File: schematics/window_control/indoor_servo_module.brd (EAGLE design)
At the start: 48.2 x 59.4 mm, 32 parts, among them J1 MTR-SERVO-FS5103B, J2 GND, J3 +5V, J4 OUTDOOR_SIGNAL, J5 J2, J6 J2, J7 J2, Q2 2N3904, Q3 2N3906BU, Q4 2N3904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

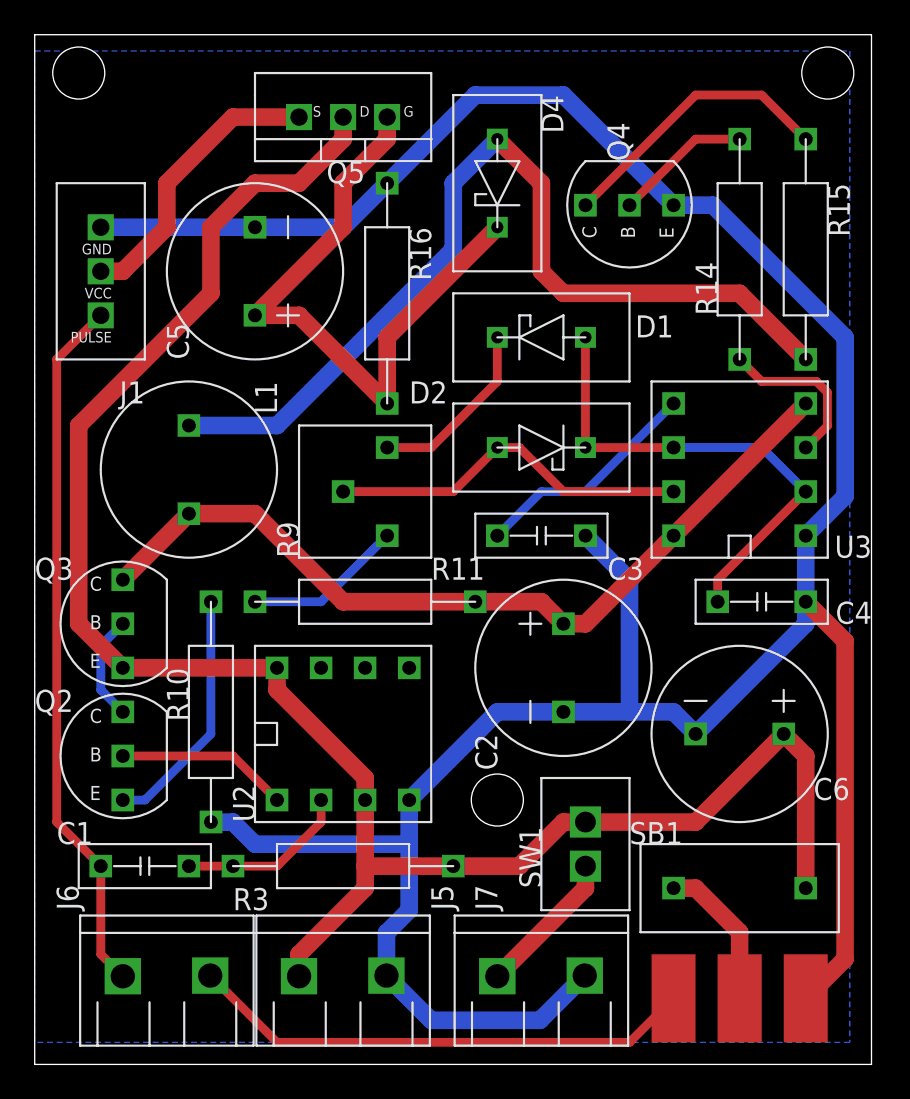
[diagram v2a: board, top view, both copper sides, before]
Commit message: Connectors changed
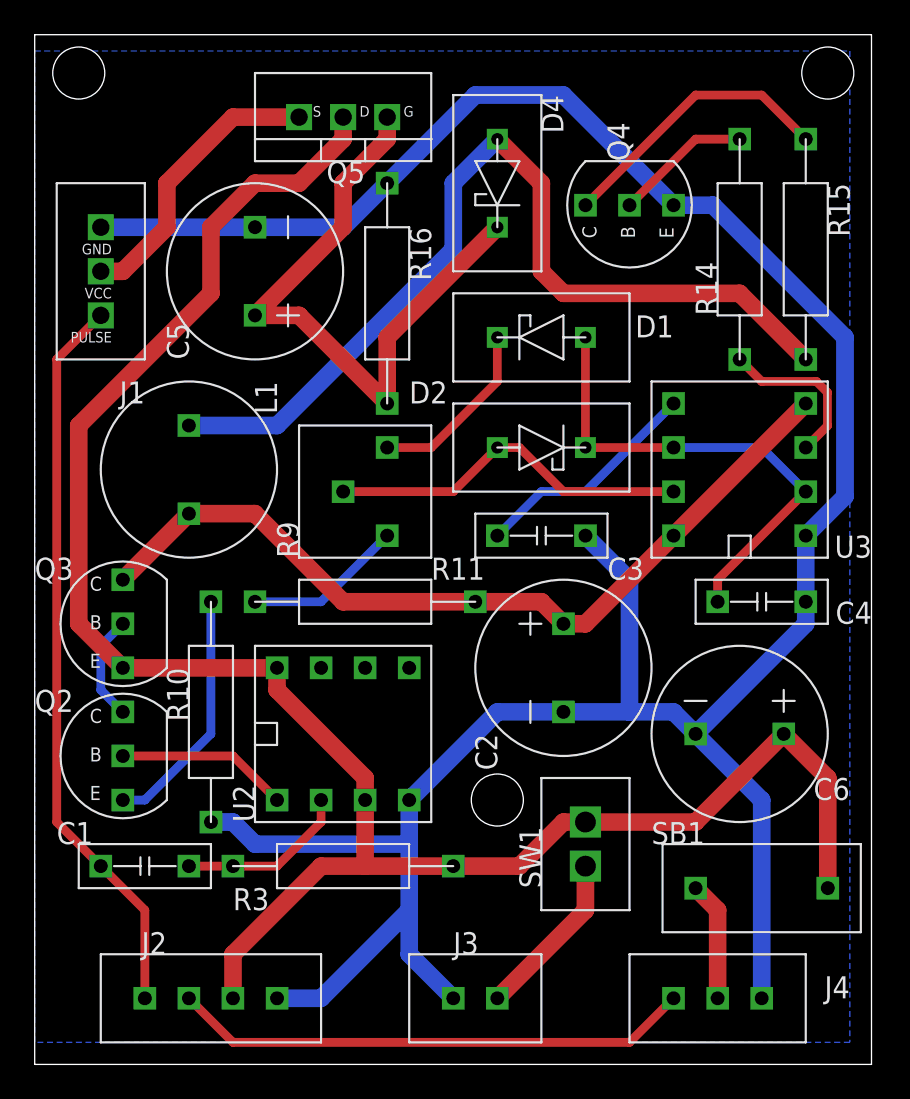
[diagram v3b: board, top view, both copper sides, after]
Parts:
- removed J5, J6, J7: J2, my_devices:J2
- J2: value GND -> JST-XH2.54-4P; device my_devices:J_SMD -> my_devices:JST-XH254-4P
- J3: value +5V -> JST-XH2.54-2P; device my_devices:J_SMD -> my_devices:JST-XH254-2P
- J4: value OUTDOOR_SIGNAL -> JST-XH2.54-3P; device my_devices:J_SMD -> my_devices:JST-XH254-3P
- moved J2 34.3 mm to (47.0, -5.08), turned to 180 degrees
- moved J3 15.2 mm to (62.2, -5.08), turned to 0 degrees
- moved J4 2.54 mm to (76.2, -5.08), turned to 180 degrees
- moved SB1 1.27 mm to (78.7, 1.27)
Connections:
- removed net N$5: J3.PIN, SB1.P$1
- new net N$4: J4.PIN2, SB1.P$1
- net +5V: now also J2.PIN2; no longer J5.PIN_1
- net GND: now also J2.PIN1, J3.PIN1, J4.PIN1; no longer J2.PIN, J5.PIN_2, J7.PIN_2
- net N$3: now also J3.PIN2; no longer J7.PIN_1
- net OUTDOOR_SIGNAL: now also J2.PIN3, J4.PIN3; no longer J4.PIN, J6.PIN_2
- net SERVO_PWM_CONTROL: now also J2.PIN4; no longer J6.PIN_1
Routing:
- net GND: track 169.6 -> 159.6 mm
- net N$5: track 8.74 -> 0.00 mm
- net N$4: track 0.00 -> 6.88 mm
- net +5V: track 107.7 -> 112.5 mm
- net SERVO_PWM_CONTROL: track 40.7 -> 42.5 mm
- net N$3: track 8.45 -> 9.72 mm
- net OUTDOOR_SIGNAL: track 29.4 -> 30.0 mm
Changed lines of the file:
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@@
 <attribute name="NAME" x="43.18" y="30.48" size="1.27" layer="21" rot="R180"/>
-</element>
-<element name="J2" library="my_devices" package="J_SMD" value="GND" x="81.28" y="-5.08" smashed="yes" rot="R90"/>
-<element name="J3" library="my_devices" package="J_SMD" value="+5V" x="77.47" y="-5.08" smashed="yes" rot="R90"/>
-<element name="J4" library="my_devices" package="J_SMD" value="OUTDOOR_SIGNAL" x="73.66" y="-5.08" smashed="yes" rot="R90"/>
-<element name="J5" library="my_devices" package="J2" value="J2" x="54.61" y="-3.81" smashed="yes" rot="R90">
-<attribute name="NAME" x="60.96" y="0" size="1.27" layer="21" rot="R90"/>
-</element>
-<element name="J6" library="my_devices" package="J2" value="J2" x="44.45" y="-3.81" smashed="yes" rot="R90">
-<attribute name="NAME" x="39.37" y="0" size="1.27" layer="21" rot="R90"/>
-</element>
-<element name="J7" library="my_devices" package="J2" value="J2" x="66.04" y="-3.81" smashed="yes" rot="R90">
-<attribute name="NAME" x="63.5" y="0" size="1.27" layer="21" rot="R90"/>
 </element>
 <element name="L1" library="my_devices" package="L-RLB0914" value="RLB0914-102KL, 1000 uH" x="45.72" y="25.4" smashed="yes" rot="R270">
@@
 <attribute name="NAME" x="52.07" y="20.32" size="1.27" layer="21" rot="R90"/>
 </element>
-<element name="SB1" library="my_devices" package="SB-NC" value="KLS7-DS-01-B-00" x="77.47" y="1.27" smashed="yes">
-<attribute name="NAME" x="71.12" y="3.81" size="1.27" layer="21"/>
+<element name="SB1" library="my_devices" package="SB-NC" value="KLS7-DS-01-B-00" x="78.74" y="1.27" smashed="yes">
+<attribute name="NAME" x="72.39" y="3.81" size="1.27" layer="21"/>
 </element>
 <element name="SW1" library="my_devices" package="SWITCH" value="SWITCH" x="68.58" y="3.81" smashed="yes" rot="R90">
@@
 <element name="D2" library="my_devices" package="D_SCHOTTKY" value="BAT41" x="66.04" y="26.67" smashed="yes">
 <attribute name="NAME" x="58.42" y="29.21" size="1.27" layer="21"/>
+</element>
+<element name="J4" library="my_devices" package="JST-XH254-3P" value="JST-XH2.54-3P" x="76.2" y="-5.08" smashed="yes" rot="R180">
+<attribute name="NAME" x="83.82" y="-3.81" size="1.27" layer="21" rot="R180"/>
+</element>
+<element name="J2" library="my_devices" package="JST-XH254-4P" value="JST-XH2.54-4P" x="46.99" y="-5.08" smashed="yes" rot="R180">
+<attribute name="NAME" x="44.45" y="-1.27" size="1.27" layer="21" rot="R180"/>
+</element>
+<element name="J3" library="my_devices" package="JST-XH254-2P" value="JST-XH2.54-2P" x="62.23" y="-5.08" smashed="yes">
+<attribute name="NAME" x="60.96" y="-2.54" size="1.27" layer="21"/>
 </element>
 </elements>
@@
 <contactref element="R3" pad="P$2"/>
 <contactref element="U2" pad="PIN_3"/>
-<contactref element="J5" pad="PIN_1"/>
 <contactref element="SW1" pad="P$2"/>
 <contactref element="SB1" pad="P$2"/>
 <contactref element="C6" pad="PIN_PLUS"/>
-<wire x1="81.28" y1="1.27" x2="81.28" y2="8.89" width="1.016" layer="1"/>
-<wire x1="81.28" y1="8.89" x2="80.01" y2="10.16" width="1.016" layer="1"/>
+<wire x1="82.55" y1="1.27" x2="82.55" y2="7.62" width="1.016" layer="1"/>
+<wire x1="82.55" y1="7.62" x2="80.01" y2="10.16" width="1.016" layer="1"/>
 <wire x1="68.58" y1="5.08" x2="74.93" y2="5.08" width="1.016" layer="1"/>
 <wire x1="74.93" y1="5.08" x2="80.01" y2="10.16" width="1.016" layer="1"/>
-<wire x1="52.07" y1="-3.81" x2="52.07" y2="-2.54" width="1.016" layer="1"/>
-<wire x1="52.07" y1="-2.54" x2="55.88" y2="1.27" width="1.016" layer="1"/>
-<wire x1="55.88" y1="1.27" x2="55.88" y2="2.54" width="1.016" layer="1"/>
 <wire x1="55.88" y1="2.54" x2="55.88" y2="6.35" width="1.016" layer="1"/>
 <wire x1="60.96" y1="2.54" x2="55.88" y2="2.54" width="1.016" layer="1"/>
@@
 <wire x1="64.77" y1="2.54" x2="67.31" y2="5.08" width="1.016" layer="1"/>
 <wire x1="67.31" y1="5.08" x2="68.58" y2="5.08" width="1.016" layer="1"/>
+<contactref element="J2" pad="PIN2"/>
+<wire x1="55.88" y1="2.54" x2="53.34" y2="2.54" width="1.016" layer="1"/>
+<wire x1="53.34" y1="2.54" x2="48.26" y2="-2.54" width="1.016" layer="1"/>
+<wire x1="48.26" y1="-2.54" x2="48.26" y2="-5.08" width="1.016" layer="1"/>
 </signal>
 <signal name="GND">
@@
 <contactref element="C2" pad="PIN_GND"/>
 <contactref element="U3" pad="PIN_1"/>
-<contactref element="J2" pad="PIN"/>
-<contactref element="J5" pad="PIN_2"/>
-<contactref element="J7" pad="PIN_2"/>
 <contactref element="C6" pad="PIN_GND"/>
-<wire x1="57.11" y1="-3.77" x2="59.69" y2="-6.35" width="1.016" layer="16"/>
-<wire x1="65.96" y1="-6.35" x2="68.54" y2="-3.77" width="1.016" layer="16"/>
-<wire x1="59.69" y1="-6.35" x2="65.96" y2="-6.35" width="1.016" layer="16"/>
-<wire x1="57.11" y1="-3.77" x2="57.11" y2="-1.31" width="1.016" layer="16"/>
-<wire x1="57.11" y1="-1.31" x2="58.42" y2="0" width="1.016" layer="16"/>
-<wire x1="58.42" y1="0" x2="58.42" y2="3.81" width="1.016" layer="16"/>
+<wire x1="58.42" y1="3.81" x2="58.42" y2="0" width="1.016" layer="16"/>
 <wire x1="58.42" y1="3.81" x2="58.42" y2="6.35" width="1.016" layer="16"/>
 <wire x1="46.99" y1="5.08" x2="48.26" y2="5.08" width="1.016" layer="16"/>
@@
 <wire x1="49.53" y1="3.81" x2="58.42" y2="3.81" width="1.016" layer="16"/>
 <wire x1="74.93" y1="10.16" x2="81.28" y2="16.51" width="1.016" layer="16"/>
-<wire x1="81.28" y1="16.51" x2="81.28" y2="17.78" width="1.016" layer="16"/>
+<wire x1="81.28" y1="17.78" x2="81.28" y2="16.51" width="1.016" layer="16"/>
 <wire x1="81.28" y1="17.78" x2="81.28" y2="21.59" width="1.016" layer="16"/>
 <wire x1="57.15" y1="41.91" x2="54.61" y2="39.37" width="1.016" layer="16"/>
@@
 <wire x1="83.546" y1="33.02" x2="75.926" y2="40.64" width="1.016" layer="16"/>
 <wire x1="75.926" y1="40.64" x2="73.66" y2="40.64" width="1.016" layer="16"/>
-<wire x1="81.28" y1="17.78" x2="83.546" y2="15.514" width="1.016" layer="1"/>
-<wire x1="83.546" y1="-2.814" x2="81.28" y2="-5.08" width="1.016" layer="1"/>
-<wire x1="83.546" y1="15.514" x2="83.546" y2="-2.814" width="1.016" layer="1"/>
 <wire x1="58.42" y1="6.35" x2="63.5" y2="11.43" width="1.016" layer="16"/>
 <wire x1="63.5" y1="11.43" x2="67.31" y2="11.43" width="1.016" layer="16"/>
@@
 <vertex x="36.83" y="-7.62"/>
 </polygon>
+<contactref element="J4" pad="PIN1"/>
+<contactref element="J2" pad="PIN1"/>
+<contactref element="J3" pad="PIN1"/>
+<wire x1="58.42" y1="0" x2="53.34" y2="-5.08" width="1.016" layer="16"/>
+<wire x1="53.34" y1="-5.08" x2="50.8" y2="-5.08" width="1.016" layer="16"/>
+<wire x1="58.42" y1="0" x2="58.42" y2="-2.54" width="1.016" layer="16"/>
+<wire x1="58.42" y1="-2.54" x2="60.96" y2="-5.08" width="1.016" layer="16"/>
+<wire x1="74.93" y1="10.16" x2="78.74" y2="6.35" width="1.016" layer="16"/>
+<wire x1="78.74" y1="6.35" x2="78.74" y2="-5.08" width="1.016" layer="16"/>
 </signal>
 <signal name="SERVO_PWM_CONTROL">
 <contactref element="J1" pad="PULSE"/>
 <contactref element="C1" pad="P$1"/>
-<contactref element="J6" pad="PIN_1"/>
-<wire x1="41.91" y1="-3.81" x2="40.64" y2="-2.54" width="0.508" layer="1"/>
-<wire x1="40.64" y1="-2.54" x2="40.64" y2="2.54" width="0.508" layer="1"/>
 <wire x1="40.64" y1="2.54" x2="38.1" y2="5.08" width="0.508" layer="1"/>
 <wire x1="38.1" y1="5.08" x2="38.1" y2="31.75" width="0.508" layer="1"/>
 <wire x1="38.1" y1="31.75" x2="40.64" y2="34.29" width="0.508" layer="1"/>
+<contactref element="J2" pad="PIN4"/>
+<wire x1="40.64" y1="2.54" x2="43.18" y2="0" width="0.508" layer="1"/>
+<wire x1="43.18" y1="0" x2="43.18" y2="-5.08" width="0.508" layer="1"/>
 </signal>
 <signal name="N$39">
@@
 </signal>
 <signal name="OUTDOOR_SIGNAL">
-<contactref element="J4" pad="PIN"/>
-<contactref element="J6" pad="PIN_2"/>
-<wire x1="46.95" y1="-3.77" x2="50.8" y2="-7.62" width="0.508" layer="1"/>
-<wire x1="50.8" y1="-7.62" x2="71.12" y2="-7.62" width="0.508" layer="1"/>
+<contactref element="J4" pad="PIN3"/>
+<contactref element="J2" pad="PIN3"/>
+<wire x1="45.72" y1="-5.08" x2="48.26" y2="-7.62" width="0.508" layer="1"/>
 <wire x1="71.12" y1="-7.62" x2="73.66" y2="-5.08" width="0.508" layer="1"/>
+<wire x1="48.26" y1="-7.62" x2="71.12" y2="-7.62" width="0.508" layer="1"/>
 </signal>
 <signal name="N$3">
-<contactref element="J7" pad="PIN_1"/>
 <contactref element="SW1" pad="P$1"/>
-<wire x1="68.58" y1="2.54" x2="68.58" y2="1.27" width="1.016" layer="1"/>
-<wire x1="68.58" y1="1.27" x2="63.5" y2="-3.81" width="1.016" layer="1"/>
-</signal>
-<signal name="N$5">
-<contactref element="J3" pad="PIN"/>
+<contactref element="J3" pad="PIN2"/>
+<wire x1="68.58" y1="2.54" x2="68.58" y2="0" width="1.016" layer="1"/>
+<wire x1="68.58" y1="0" x2="63.5" y2="-5.08" width="1.016" layer="1"/>
+</signal>
+<signal name="N$4">
+<contactref element="J4" pad="PIN2"/>
 <contactref element="SB1" pad="P$1"/>
-<wire x1="77.4192" y1="-5.0292" x2="77.47" y2="-5.08" width="0.1524" layer="1"/>
-<wire x1="77.47" y1="-5.08" x2="77.47" y2="-1.27" width="1.016" layer="1"/>
-<wire x1="77.47" y1="-1.27" x2="74.93" y2="1.27" width="1.016" layer="1"/>
-<wire x1="74.93" y1="1.27" x2="73.66" y2="1.27" width="1.016" layer="1"/>
+<wire x1="74.93" y1="1.27" x2="76.2" y2="0" width="1.016" layer="1"/>
+<wire x1="76.2" y1="0" x2="76.2" y2="-5.08" width="1.016" layer="1"/>
 </signal>
 </signals>

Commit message: Fixed issue in one border - all supply lines now connected to capacity only. And from filter capacity power goes to another elements.
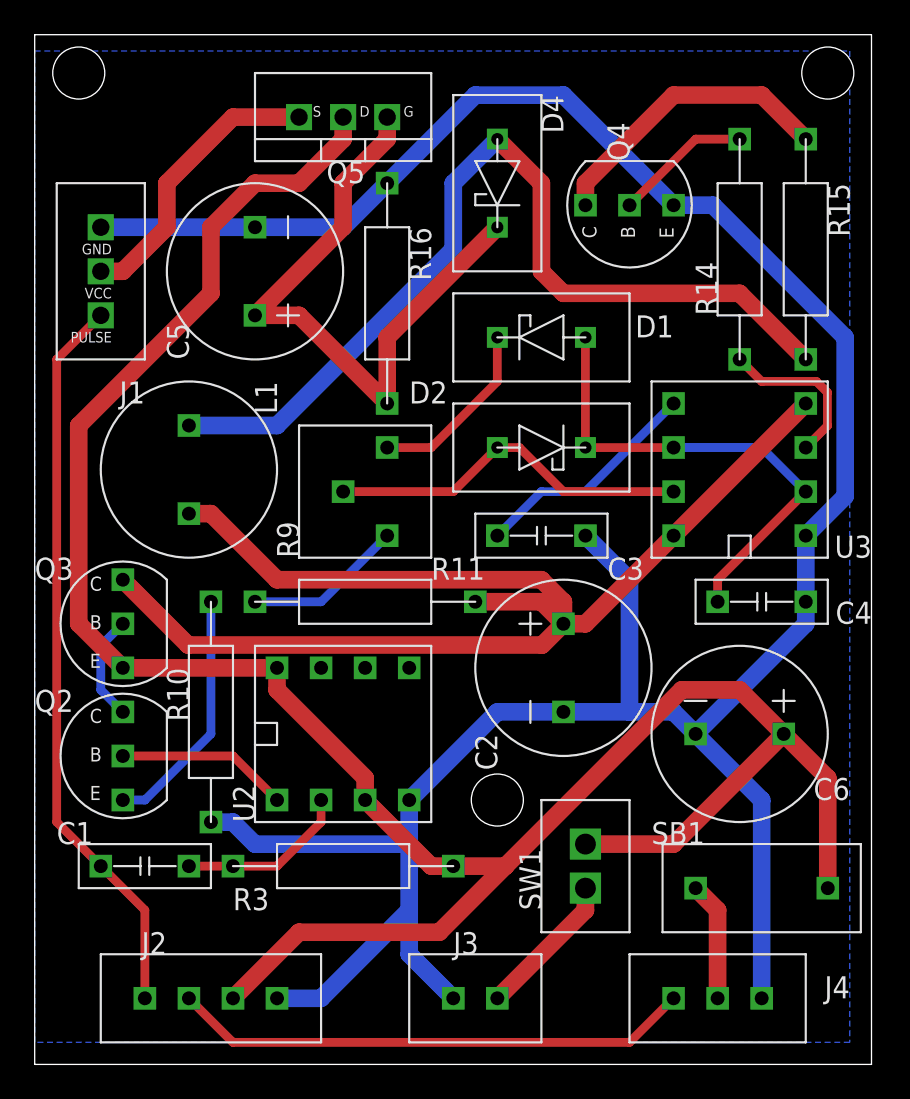
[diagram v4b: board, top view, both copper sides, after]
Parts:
- moved SW1 1.27 mm to (68.6, 2.54)
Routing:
- net +5V_IF_EN: track 48.8 -> 77.3 mm
- net +5V: track 112.5 -> 133.1 mm
- net N$3: track 9.72 -> 8.45 mm
- net N$1: track 16.4 -> 17.1 mm
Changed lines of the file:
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@@
 <drawing>
 <settings>
-<setting alwaysvectorfont="no"/>
+<setting alwaysvectorfont="yes"/>
 <setting verticaltext="up"/>
 </settings>
@@
 <attribute name="NAME" x="72.39" y="3.81" size="1.27" layer="21"/>
 </element>
-<element name="SW1" library="my_devices" package="SWITCH" value="SWITCH" x="68.58" y="3.81" smashed="yes" rot="R90">
-<attribute name="NAME" x="66.04" y="1.27" size="1.27" layer="21" rot="R90"/>
+<element name="SW1" library="my_devices" package="SWITCH" value="SWITCH" x="68.58" y="2.54" smashed="yes" rot="R90">
+<attribute name="NAME" x="66.04" y="0" size="1.27" layer="21" rot="R90"/>
 </element>
 <element name="U2" library="my_devices" package="DIP8" value="LM311P" x="54.61" y="10.16" smashed="yes" rot="R90">
@@
 <wire x1="82.55" y1="1.27" x2="82.55" y2="7.62" width="1.016" layer="1"/>
 <wire x1="82.55" y1="7.62" x2="80.01" y2="10.16" width="1.016" layer="1"/>
-<wire x1="68.58" y1="5.08" x2="74.93" y2="5.08" width="1.016" layer="1"/>
-<wire x1="74.93" y1="5.08" x2="80.01" y2="10.16" width="1.016" layer="1"/>
-<wire x1="55.88" y1="2.54" x2="55.88" y2="6.35" width="1.016" layer="1"/>
-<wire x1="60.96" y1="2.54" x2="55.88" y2="2.54" width="1.016" layer="1"/>
+<wire x1="68.58" y1="3.81" x2="73.66" y2="3.81" width="1.016" layer="1"/>
+<wire x1="73.66" y1="3.81" x2="80.01" y2="10.16" width="1.016" layer="1"/>
 <wire x1="55.88" y1="6.35" x2="55.88" y2="7.62" width="1.016" layer="1"/>
 <wire x1="50.8" y1="12.7" x2="50.8" y2="13.97" width="1.016" layer="1"/>
@@
 <wire x1="54.61" y1="44.45" x2="54.61" y2="45.72" width="1.016" layer="1"/>
 <wire x1="39.37" y1="27.94" x2="46.99" y2="35.56" width="1.016" layer="1"/>
-<wire x1="60.96" y1="2.54" x2="64.77" y2="2.54" width="1.016" layer="1"/>
-<wire x1="64.77" y1="2.54" x2="67.31" y2="5.08" width="1.016" layer="1"/>
-<wire x1="67.31" y1="5.08" x2="68.58" y2="5.08" width="1.016" layer="1"/>
 <contactref element="J2" pad="PIN2"/>
-<wire x1="55.88" y1="2.54" x2="53.34" y2="2.54" width="1.016" layer="1"/>
-<wire x1="53.34" y1="2.54" x2="48.26" y2="-2.54" width="1.016" layer="1"/>
-<wire x1="48.26" y1="-2.54" x2="48.26" y2="-5.08" width="1.016" layer="1"/>
+<wire x1="77.47" y1="12.7" x2="80.01" y2="10.16" width="1.016" layer="1"/>
+<wire x1="77.47" y1="12.7" x2="74.1265875" y2="12.7" width="1.016" layer="1"/>
+<wire x1="63.9665875" y1="2.54" x2="60.96" y2="2.54" width="1.016" layer="1"/>
+<wire x1="74.1265875" y1="12.7" x2="63.9665875" y2="2.54" width="1.016" layer="1"/>
+<wire x1="60.96" y1="2.54" x2="59.69" y2="2.54" width="1.016" layer="1"/>
+<wire x1="59.69" y1="2.54" x2="55.88" y2="6.35" width="1.016" layer="1"/>
+<wire x1="48.26" y1="-5.08" x2="52.07" y2="-1.27" width="1.016" layer="1"/>
+<wire x1="60.1565875" y1="-1.27" x2="63.9665875" y2="2.54" width="1.016" layer="1"/>
+<wire x1="52.07" y1="-1.27" x2="60.1565875" y2="-1.27" width="1.016" layer="1"/>
 </signal>
 <signal name="GND">
@@
 <contactref element="U3" pad="PIN_4"/>
 <contactref element="U3" pad="PIN_8"/>
-<wire x1="41.91" y1="19.05" x2="45.72" y2="22.86" width="1.016" layer="1"/>
-<wire x1="45.72" y1="22.86" x2="49.53" y2="22.86" width="1.016" layer="1"/>
-<wire x1="54.61" y1="17.78" x2="62.23" y2="17.78" width="1.016" layer="1"/>
-<wire x1="49.53" y1="22.86" x2="54.61" y2="17.78" width="1.016" layer="1"/>
 <wire x1="73.66" y1="21.59" x2="81.28" y2="29.21" width="1.016" layer="1"/>
 <wire x1="62.23" y1="17.78" x2="66.04" y2="17.78" width="1.016" layer="1"/>
@@
 <wire x1="73.66" y1="21.59" x2="68.58" y2="16.51" width="1.016" layer="1"/>
 <wire x1="68.58" y1="16.51" x2="67.31" y2="16.51" width="1.016" layer="1"/>
+<wire x1="67.2656" y1="16.4656" x2="67.31" y2="16.51" width="1.016" layer="1"/>
+<wire x1="41.91" y1="19.05" x2="45.6756" y2="15.2844" width="1.016" layer="1"/>
+<wire x1="66.0844" y1="15.2844" x2="67.31" y2="16.51" width="1.016" layer="1"/>
+<wire x1="45.6756" y1="15.2844" x2="66.0844" y2="15.2844" width="1.016" layer="1"/>
+<wire x1="67.31" y1="16.51" x2="67.31" y2="17.78" width="1.016" layer="1"/>
+<wire x1="67.31" y1="17.78" x2="66.04" y2="19.05" width="1.016" layer="1"/>
+<wire x1="50.8" y1="19.05" x2="46.99" y2="22.86" width="1.016" layer="1"/>
+<wire x1="46.99" y1="22.86" x2="45.72" y2="22.86" width="1.016" layer="1"/>
+<wire x1="66.04" y1="19.05" x2="50.8" y2="19.05" width="1.016" layer="1"/>
 </signal>
 <signal name="N$35">
@@
 <contactref element="Q4" pad="C"/>
 <contactref element="R15" pad="P$1"/>
-<wire x1="68.58" y1="40.64" x2="74.93" y2="46.99" width="0.508" layer="1"/>
-<wire x1="78.74" y1="46.99" x2="81.28" y2="44.45" width="0.508" layer="1"/>
-<wire x1="74.93" y1="46.99" x2="78.74" y2="46.99" width="0.508" layer="1"/>
+<wire x1="68.58" y1="40.64" x2="68.58" y2="41.91" width="1.016" layer="1"/>
+<wire x1="73.66" y1="46.99" x2="78.74" y2="46.99" width="1.016" layer="1"/>
+<wire x1="78.74" y1="46.99" x2="81.28" y2="44.45" width="1.016" layer="1"/>
+<wire x1="68.58" y1="41.91" x2="73.66" y2="46.99" width="1.016" layer="1"/>
 </signal>
 <signal name="N$2">
@@
 <contactref element="SW1" pad="P$1"/>
 <contactref element="J3" pad="PIN2"/>
-<wire x1="68.58" y1="2.54" x2="68.58" y2="0" width="1.016" layer="1"/>
+<wire x1="68.58" y1="1.27" x2="68.58" y2="0" width="1.016" layer="1"/>
 <wire x1="68.58" y1="0" x2="63.5" y2="-5.08" width="1.016" layer="1"/>
 </signal>
